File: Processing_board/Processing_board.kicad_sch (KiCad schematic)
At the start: 29 parts, among them J1 Conn_01x08_Pin, J12 Conn_01x02_Pin, J2 Conn_01x08_Pin, J3 Conn_01x06_Pin, J4 Conn_01x03_Pin, J5 Conn_01x03_Pin, J6 Conn_01x02_Pin, SW1 TL3305BF100QG, SW2 TL3305BF100QG, U1 STM32WBA63CIU6

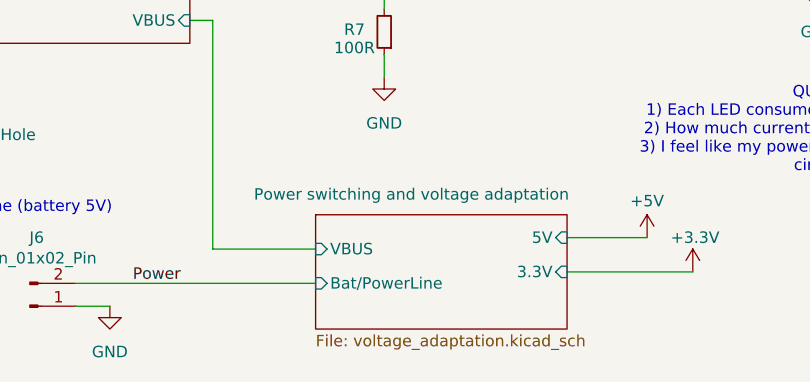
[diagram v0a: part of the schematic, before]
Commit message: Add the new power supply and connect the ADCs at the GND an power
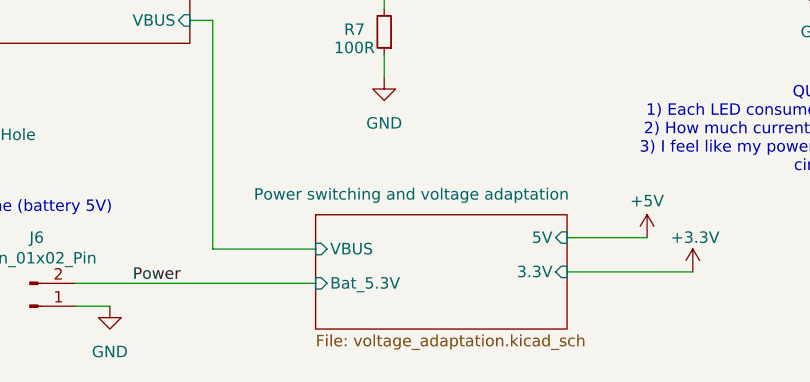
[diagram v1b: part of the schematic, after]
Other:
- sheet Power switching and voltage adaptation ports: added Bat_5.3V; removed Bat/PowerLine
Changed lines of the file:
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@@
 			)
 		)
-		(pin "Bat{slash}PowerLine" input
+		(pin "Bat_5.3V" input
 			(at 87.63 184.15 180)
 			(effects
